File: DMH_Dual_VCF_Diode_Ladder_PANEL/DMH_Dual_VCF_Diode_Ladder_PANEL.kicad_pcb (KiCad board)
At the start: 2 copper layers, 150 x 200 mm, 43 parts, among them J0 Panel_GND_Solder_Wire_Pad

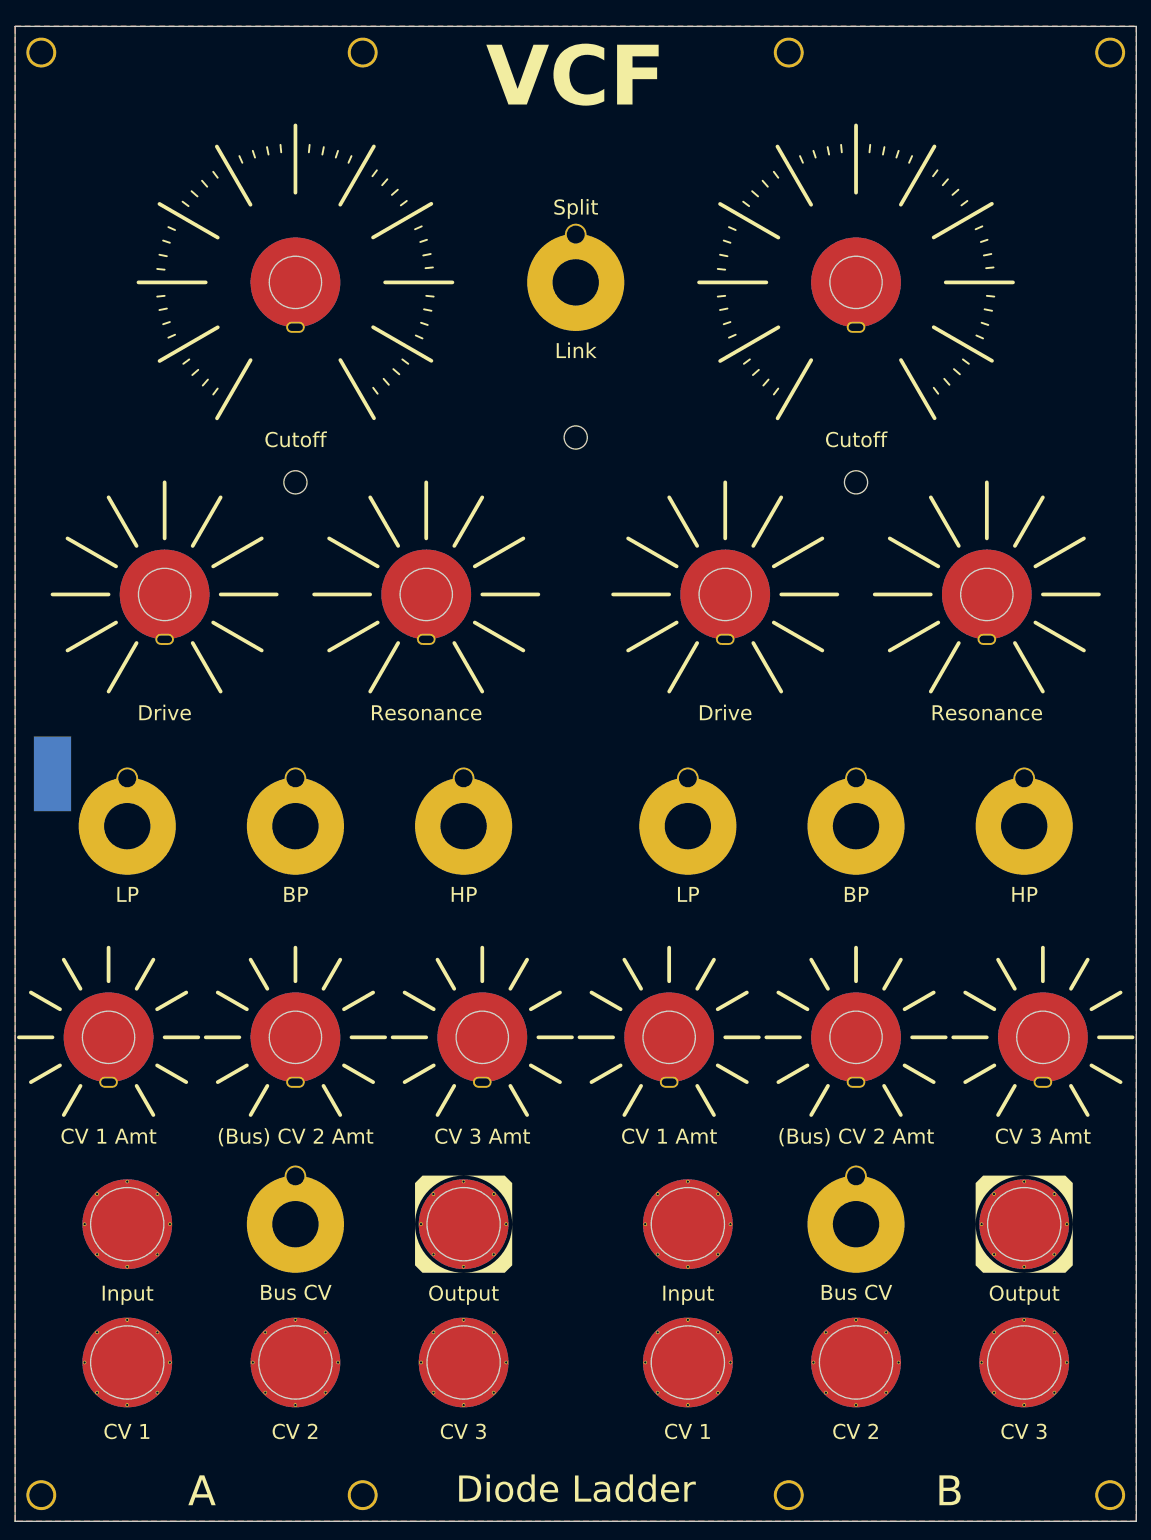
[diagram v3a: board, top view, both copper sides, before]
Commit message: Added central cutoff knob
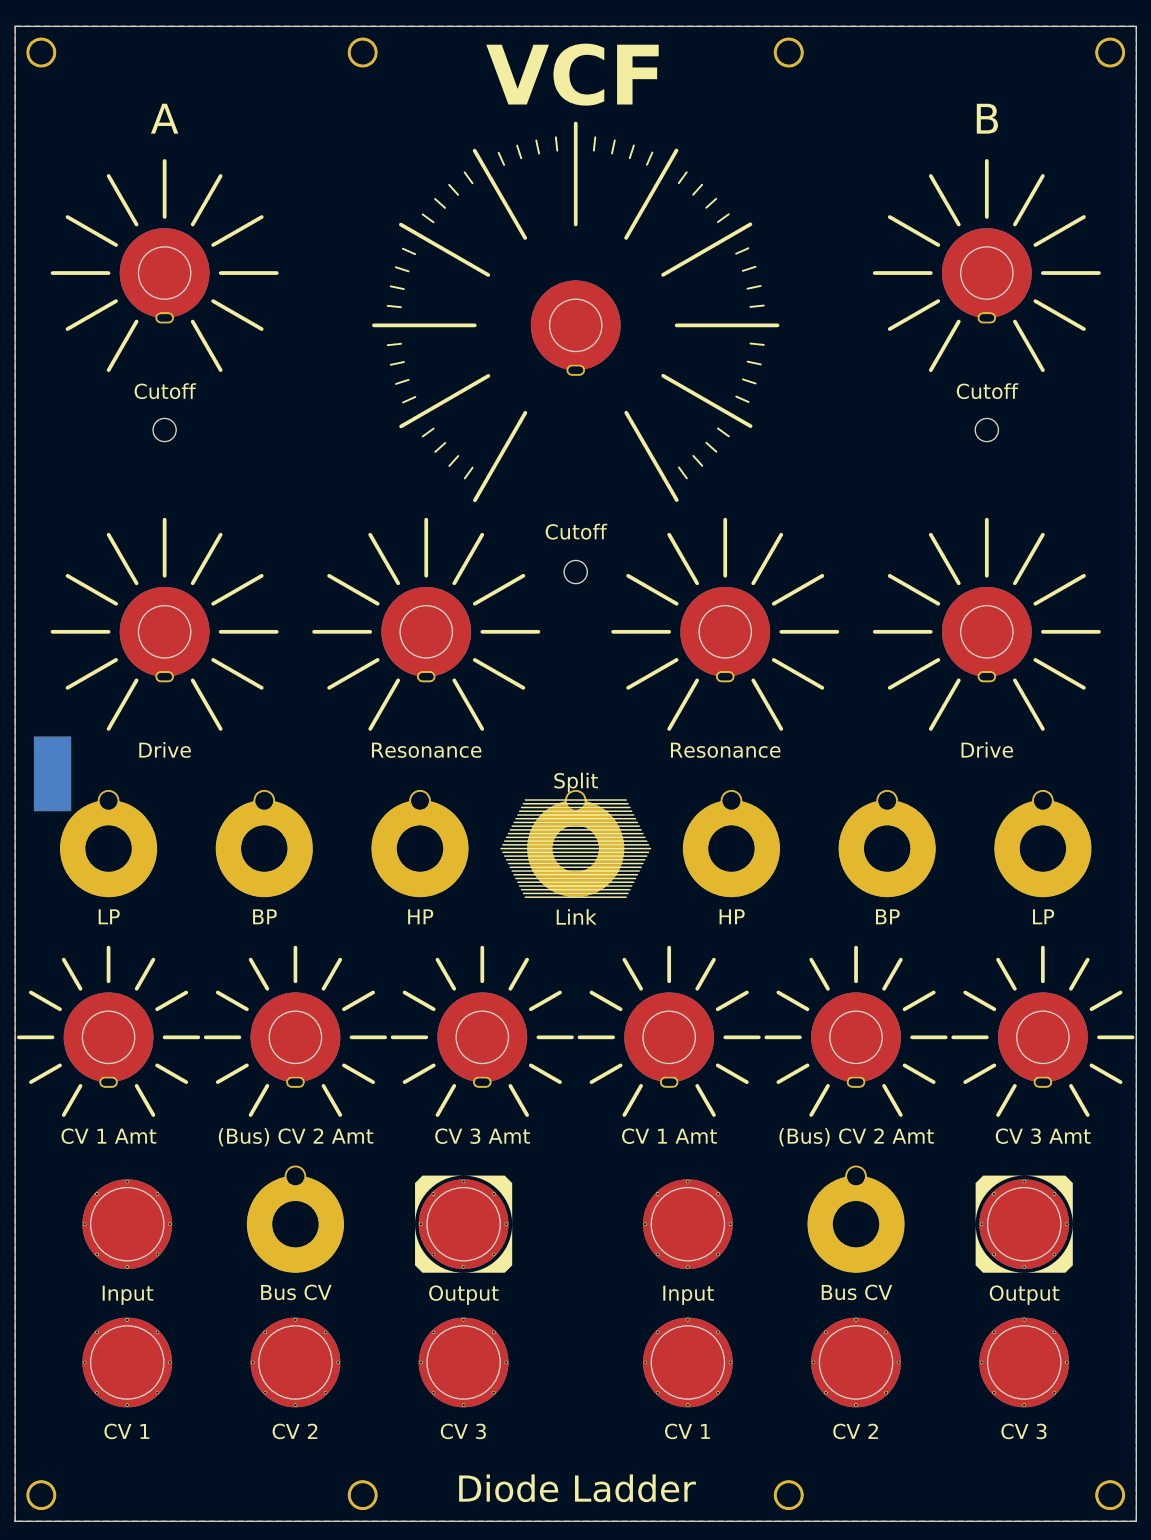
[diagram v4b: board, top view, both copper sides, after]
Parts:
- added H43: Cutoff, SynthStuff:Pot_Cutout_Huge_v2, F.Cu at (100.0, 70.0)
- H27, H9: footprint SynthStuff:Pot_Cutout_Large_v2 -> SynthStuff:Pot_Cutout_Small
- moved H33 75.8 mm to (100.0, 140.0)
- moved H24 47.6 mm to (162.5, 140.0)
- moved H35 39.3 mm to (120.8, 140.0)
- moved H21 35.4 mm to (155.0, 111.0)
- moved H31 35.4 mm to (120.0, 111.0)
- moved H40 18.8 mm to (45.0, 84.0)
- moved H42 18.8 mm to (155.0, 84.0)
- moved H41 18.0 mm to (100.0, 103.0)
- moved H27 17.5 mm to (155.0, 63.0)
- moved H9 17.5 mm to (45.0, 63.0)
- moved H26 6.56 mm to (79.2, 140.0)
- moved H20 5.13 mm to (58.3, 140.0)
- moved H34 5.13 mm to (141.7, 140.0)
- moved H10 5.00 mm to (45.0, 111.0)
- moved H11 5.00 mm to (80.0, 111.0)
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
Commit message: Changed features on panel
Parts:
- H13, H32: value CV 3 Amt -> Res CV Amt
- H17, H28: value (Bus) CV 2 Amt -> CV 2 Amt
- H27, H9: footprint SynthStuff:Pot_Cutout_Small -> SynthStuff:Pot_Cutout_Medium_v2
- H29, H7: value CV 3 -> Res CV
- moved H40 4.00 mm to (45.0, 88.0)
- moved H42 4.00 mm to (155.0, 88.0)
- moved H27 1.00 mm to (155.0, 64.0)
- moved H9 1.00 mm to (45.0, 64.0)
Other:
- board text added: "1/2"
- board text added: "Off"
- board text added: "V/Oct"

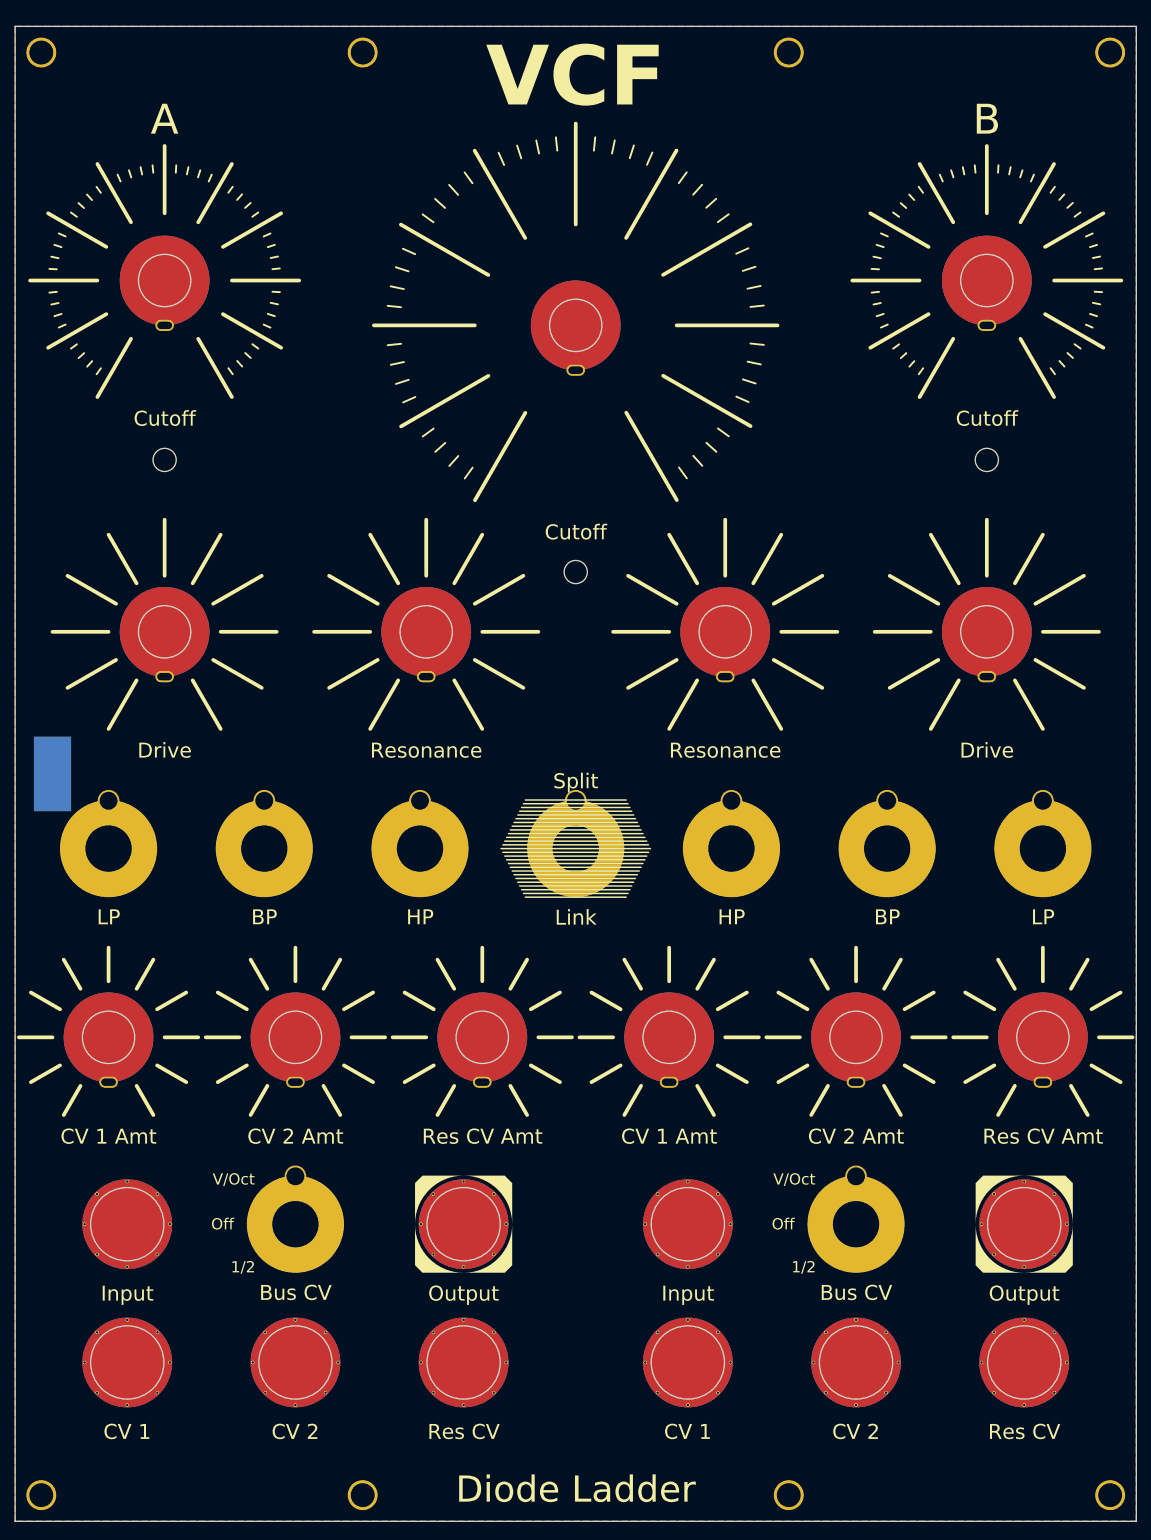
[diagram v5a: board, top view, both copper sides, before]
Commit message: Reorganized panel
... and added Feed switch.
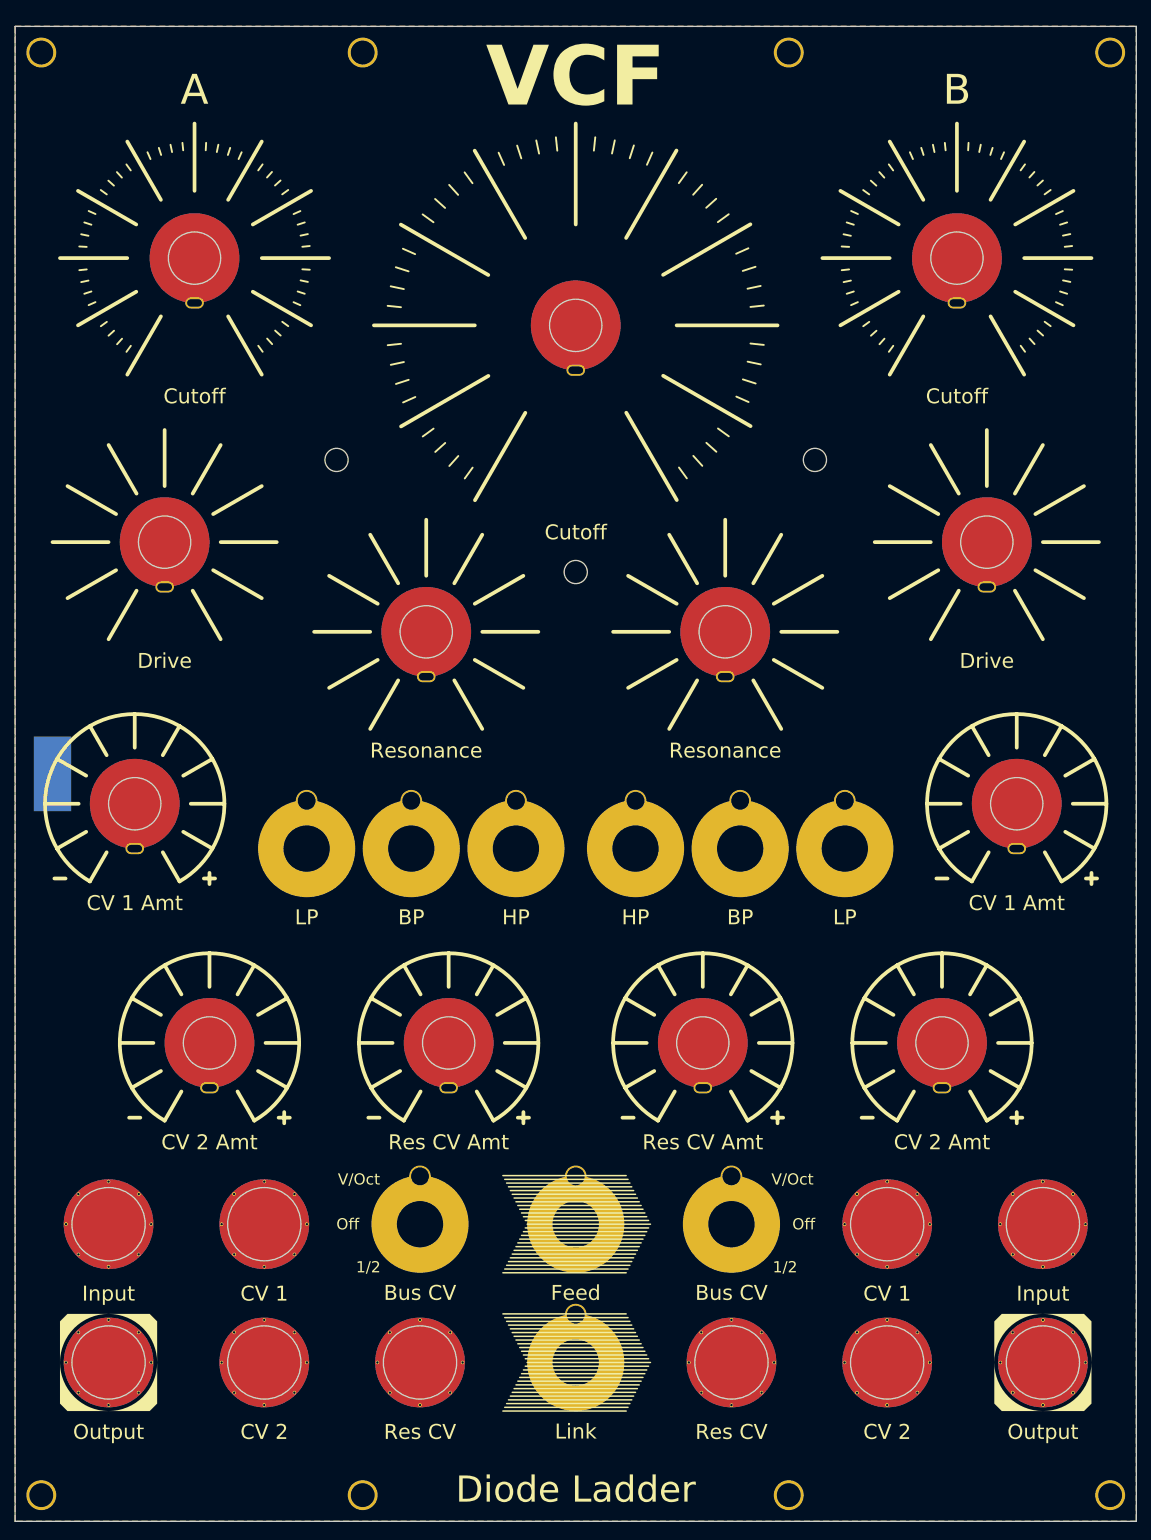
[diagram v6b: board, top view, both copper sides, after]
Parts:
- added H44: Feed, SynthStuff:Toggle_Switch_Cutout, F.Cu at (100.0, 190.2)
- H12, H13, H17, H22, H28, H32: footprint SynthStuff:Pot_Cutout_Tiny -> SynthStuff:Pot_Cutout_Tiny_attv
- moved H33 68.8 mm to (100.0, 208.8)
- moved H22 56.0 mm to (159.0, 134.0)
- moved H8 51.0 mm to (37.5, 208.8)
- moved H16 47.5 mm to (162.5, 190.2)
- moved H32 45.5 mm to (117.0, 166.0)
- moved H29 39.2 mm to (120.8, 208.8)
- moved H15 32.5 mm to (141.7, 190.2)
- moved H12 31.4 mm to (41.0, 134.0)
- moved H14 26.5 mm to (64.0, 140.0)
- moved H24 26.5 mm to (136.0, 140.0)
- moved H6 26.0 mm to (58.3, 190.2)
- moved H40 23.0 mm to (68.0, 88.0)
- moved H42 23.0 mm to (132.0, 88.0)
- moved H20 19.7 mm to (78.0, 140.0)
- moved H34 19.7 mm to (122.0, 140.0)
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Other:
- board text removed: "Split"
